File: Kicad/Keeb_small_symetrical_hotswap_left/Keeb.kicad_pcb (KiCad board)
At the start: 2 copper layers, 96.2 x 97.6 mm, 30 parts, among them J1 TYPE-C-31-M-12, SW1 CherryMX, SW10 CherryMX, SW11 CherryMX, SW13 CherryMX, SW14 CherryMX, SW15 CherryMX, SW16 CherryMX, SW17 CherryMX, SW18 CherryMX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

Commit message: added a connectior for the battery
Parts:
- added J2: B2B-XH-A_LF__SN_, Connectors_user:JST_B2B-XH-A_LF__SN_, F.Cu at (141.6, 85.1)
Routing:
- net GND: track 599.1 -> 653.3 mm
- net 18: track 53.0 -> 47.0 mm
- net 19: track 77.8 -> 72.0 mm
- net 3v3: track 282.0 -> 286.7 mm
- net VSYS: track 116.3 -> 119.0 mm
- net 16: track 74.2 -> 72.7 mm
- net 15: track 60.2 -> 59.1 mm
- net 17: track 57.7 -> 57.0 mm
- net 22: track 61.6 -> 61.0 mm
- net 14: track 63.0 -> 63.6 mm

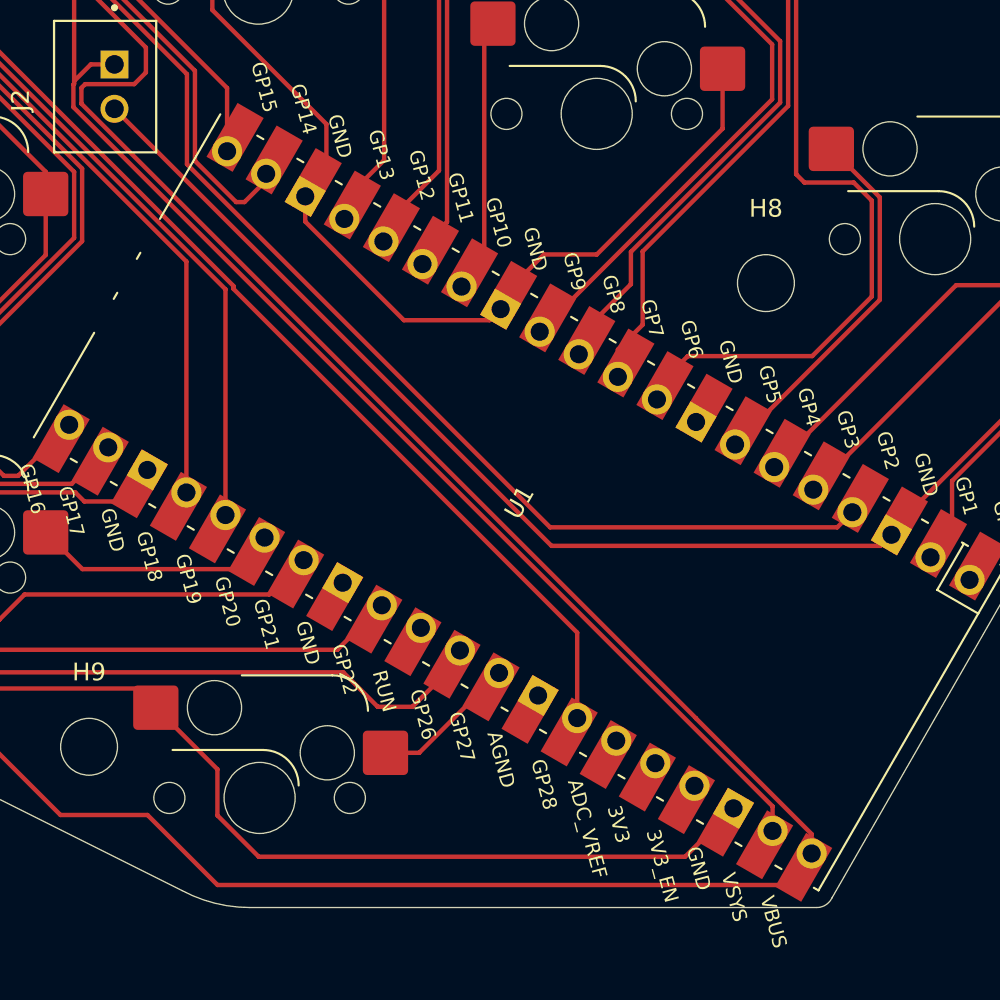
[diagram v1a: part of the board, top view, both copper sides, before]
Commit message: added a on/off
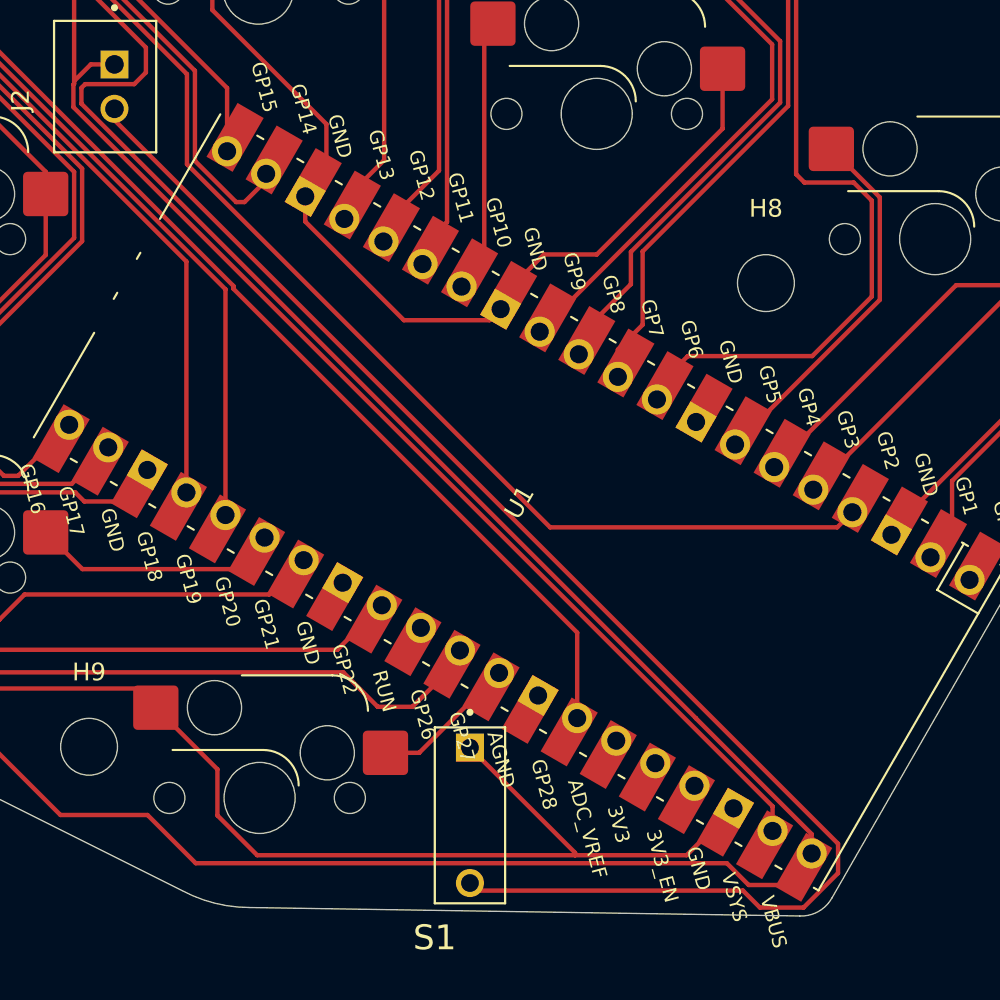
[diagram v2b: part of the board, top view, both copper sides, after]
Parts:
- added S1: DS01-254-L-01BE, DIP:SW_DS01-254-L-01BE, F.Cu at (162.1, 126.2)
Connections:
- J2 pad 2: GND -> Net-(J2-Pad2)
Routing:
- net Net-(J2-Pad2): track 0.00 -> 81.8 mm
- net GND: track 653.3 -> 607.6 mm
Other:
- board size 96.2 x 97.6 mm -> 96.2 x 98.1 mm

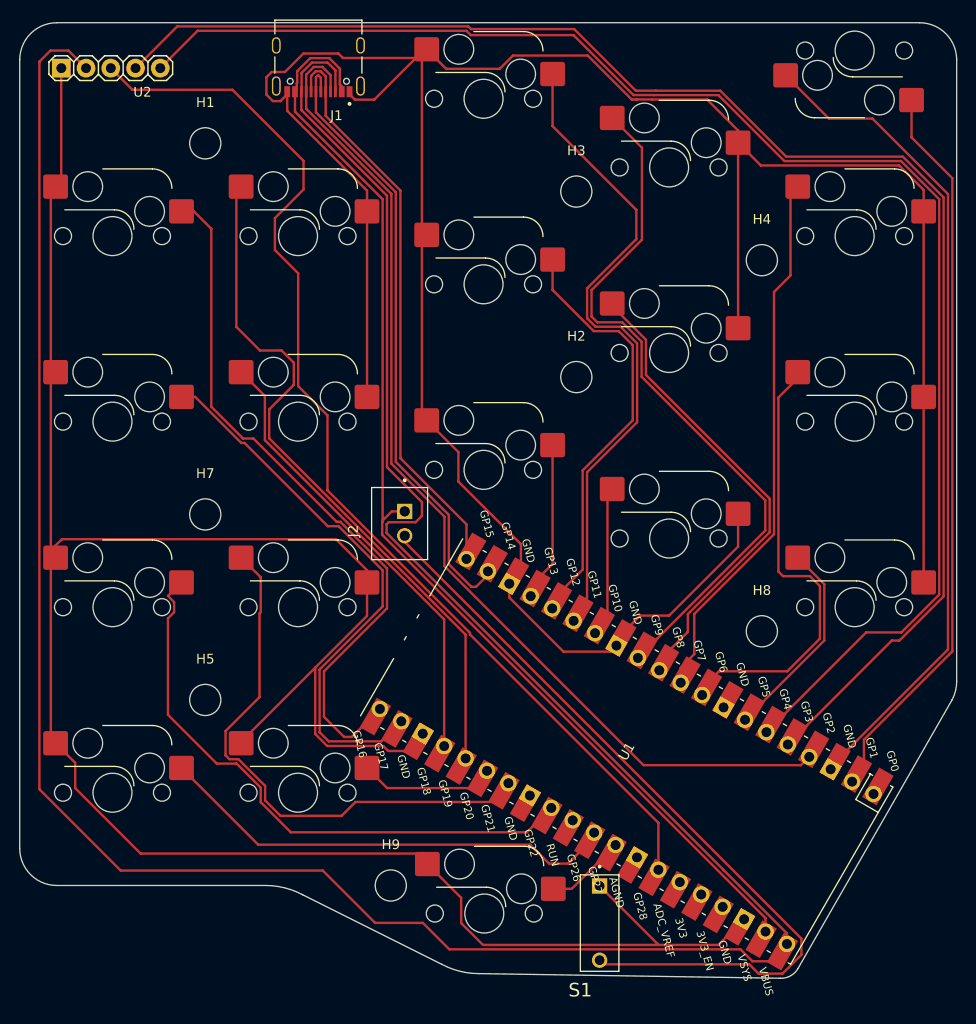
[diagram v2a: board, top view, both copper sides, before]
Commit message: Switched footprint to copper plater one to give an opiton of soldering switches directly
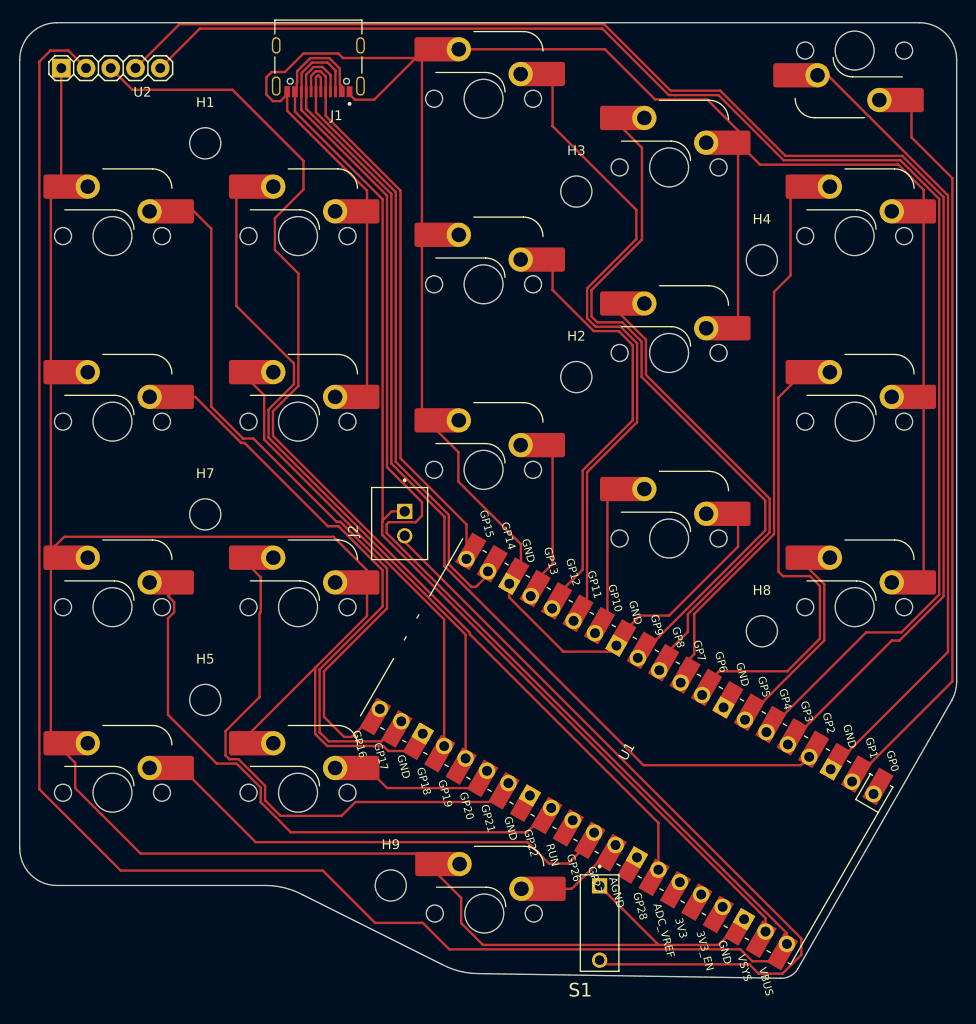
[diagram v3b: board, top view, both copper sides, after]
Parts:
- SW1, SW10, SW11, SW13, SW14, SW15, SW16, SW17, SW18, SW19, SW2, SW20, SW3, SW4, SW5, SW6, SW7, SW8, SW9: footprint ScottoKeebs_Hotswap:Hotswap_MX_1.00u -> ScottoKeebs_Hotswap:Hotswap_MX_Plated_1.00u_Smaller_hole
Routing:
- net 28: track 114.0 -> 116.2 mm
- net 19: track 72.0 -> 70.8 mm
- net GND: track 607.6 -> 606.6 mm
